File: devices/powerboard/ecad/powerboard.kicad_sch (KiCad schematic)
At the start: 40 parts, among them J1 Conn_02x02_Top_Bottom, J10 Conn_02x01, J2 Conn_02x02_Top_Bottom, J3 Conn_02x01, J4 Conn_02x01, J5 USB_A, J6 JST PH, J7 JST PH, J8 47053-1000, J9 USB_A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

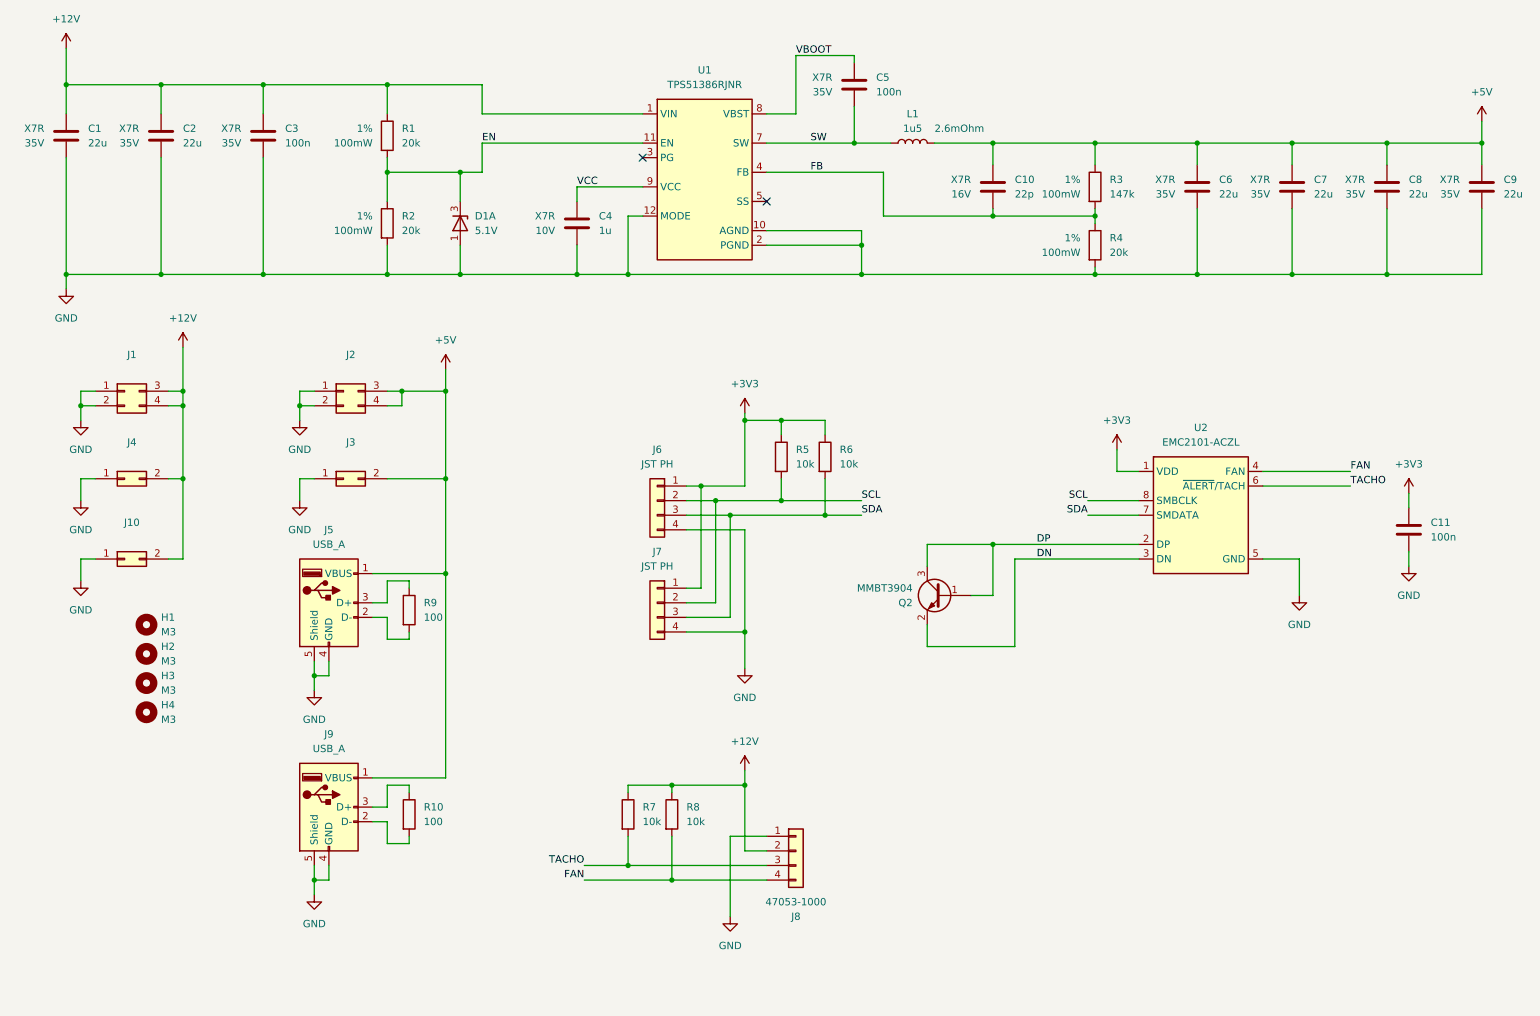
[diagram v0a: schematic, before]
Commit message: [WIP][powerboard] changes the inductor
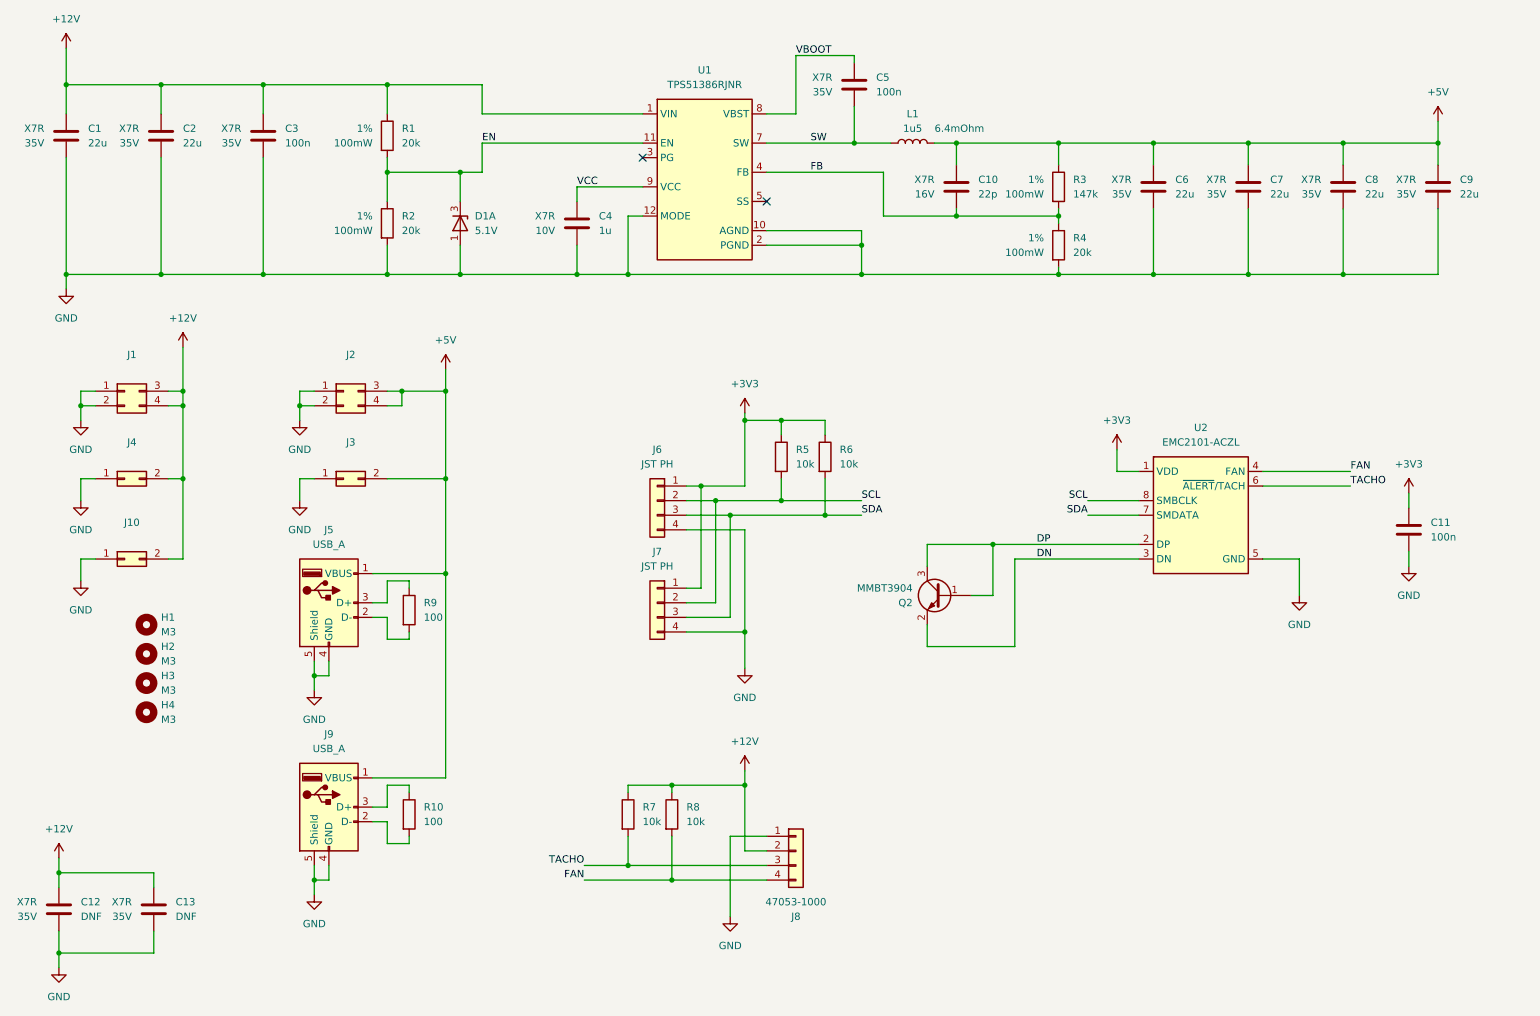
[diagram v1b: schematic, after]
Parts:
- added C12, C13: DNF, Capacitor_SMD:C_1206_3216Metric, symbol Device:C
- L1: footprint common:L_Bourns_SRP1270_13.7x13.7mm -> common:L_Bourns_SRP6050CA_6.6x6.4mm; DSR 2.6mOhm -> 6.4mOhm; MPN (none) -> SRP6050CA-1R5M
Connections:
- net +12V: now also C12.1, C13.1
- net GND: now also C12.2, C13.2
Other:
- moved on the sheet: C10, C6, C7, C8, C9, R3, R4

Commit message: Powerboard revA done
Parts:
- added C14: DNF, Capacitor_SMD:C_0603_1608Metric, symbol Device:C
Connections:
- net +5V: now also C14.1
- net GND: now also C14.2
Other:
- moved on the sheet: C1, C10, C11, C2, C3, C4, C5, C6, C7, C8, C9, D1A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

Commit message: Updates power distribution board
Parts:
- removed H1, H2, H3, H4: M3, MountingHole:MountingHole_3.2mm_M3, symbol Mechanical:MountingHole
- removed J10: Conn_02x01, Connector_Molex:Molex_Mini-Fit_Jr_5569-02A2_2x01_P4.20mm_Horizontal, symbol Connector_Generic:Conn_02x01
- removed J9: USB_A, common:AMP_87583-2010RPLF, symbol Connector:USB_A
- removed R10: 100, Resistor_SMD:R_0805_2012Metric, symbol Device:R
- removed R5, R6: 10k, Resistor_SMD:R_0805_2012Metric, symbol Device:R
- added C15: 56n, Capacitor_SMD:C_0603_1608Metric, symbol Device:C
- added J10: S2B-PH-K, Connector_JST:JST_PH_S2B-PH-K_1x02_P2.00mm_Horizontal, symbol Connector_Generic:Conn_01x02
- added J9: S4B-PH-SM4-TB, common:JST_PH_S4B-PH-SM4-TB_1x04-1MP_P2.00mm_Horizontal, symbol Connector_Generic:Conn_01x04
- added JP1: Jumper_2_Open, Connector_PinHeader_2.54mm:PinHeader_1x02_P2.54mm_Vertical, symbol Jumper:Jumper_2_Open
- C12, C13: value DNF -> 22u; now not fitted
- C14: value DNF -> 100n; now not fitted
- J1, J2: footprint Connector_Molex:Molex_Mini-Fit_Jr_5569-04A2_2x02_P4.20mm_Horizontal -> common:Molex_Mini-Fit_Jr_5569-04A2_2x02_P4.20mm_Horizontal
- J3, J4: footprint Connector_Molex:Molex_Mini-Fit_Jr_5569-02A2_2x01_P4.20mm_Horizontal -> common:Molex_Mini-Fit_Jr_5569-02A2_2x01_P4.20mm_Horizontal
- J6, J7: value JST PH -> SM04-SRSS-TB; footprint common:JST_PH_S4B-PH-SM4-TB_1x04-1MP_P2.00mm_Horizontal -> common:JST_SH_SM04B-SRSS-TB_1x04-1MP_P1.00mm_Horizontal
- R7, R8: now not fitted
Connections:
- net +12V: now also J10.1 (Pin_1)
- net +3V3: now also J6.2 (Pin_2), J7.2 (Pin_2), JP1.1 (A); no longer J6.1 (Pin_1), J7.1 (Pin_1)
- net GND: now also J6.1 (Pin_1), J7.1 (Pin_1), C15.2, J10.2 (Pin_2), J9.4 (Pin_4); no longer J6.4 (Pin_4), J7.4 (Pin_4)
- net SCL: now also J6.4 (Pin_4), J7.4 (Pin_4), J9.2 (Pin_2); no longer J6.2 (Pin_2), J7.2 (Pin_2)
- net SDA: now also J9.3 (Pin_3)
- net at U1.5 (SS): now also C15.1
- new net: J9.1 (Pin_1), JP1.2 (B)
- no-connect marks 2 -> 1
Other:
- moved on the sheet: J6, J8, R9

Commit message: Conforms all board together
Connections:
- net BOOT: now reaches C15.1, U1.5 (SS)
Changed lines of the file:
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@@
+		)
+	)
+	(label "BOOT"
+		(at 156.21 48.26 0)
+		(fields_autoplaced yes)
+		(effects
+			(font
+				(size 1.27 1.27)
+			)
+			(justify left bottom)
 		)
 	)
